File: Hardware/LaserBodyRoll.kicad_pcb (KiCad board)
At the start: 2 copper layers, 85 parts, among them J1 CONN_01X02, J2 FTSH-105-01-L-DV-K, J4 CONN_01X06, J5 CONN_01X02, J6 CONN_01X02, J7 CONN_01X06, J8 Raspberry_Pi_2_3, Q1 Q_NPN_BCE, Q2 Q_NPN_BCE, Q3 Q_NPN_BCE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

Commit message: Updated the board outline and placement of parts.
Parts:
- removed C6: 0.1u, Capacitors_SMD:C_0603
- removed J7: CONN_01X06, Connectors_Phoenix:PhoenixContact_MSTBVA-G_06x5.00mm_Vertical
- added J3: Conn_01x04, Pin_Headers:Pin_Header_Straight_1x04_Pitch2.54mm, F.Cu at (101.4, 78.0)
- added REF**: MountingHole_2.7mm_M2.5, Mounting_Holes:MountingHole_2.7mm_M2.5, F.Cu at (56.0, 67.0)
- added REF**: MountingHole_2.7mm_M2.5, Mounting_Holes:MountingHole_2.7mm_M2.5, F.Cu at (114.0, 44.0)
- added REF**: MountingHole_2.7mm_M2.5, Mounting_Holes:MountingHole_2.7mm_M2.5, F.Cu at (56.0, 44.0)
- added REF**: MountingHole_3.2mm_M3, Mounting_Holes:MountingHole_3.2mm_M3, F.Cu at (140.0, 44.0)
- added REF**: MountingHole_3.2mm_M3, Mounting_Holes:MountingHole_3.2mm_M3, F.Cu at (140.0, 76.0)
- added REF**: MountingHole_3.2mm_M3, Mounting_Holes:MountingHole_3.2mm_M3, F.Cu at (44.0, 76.0)
- added REF**: MountingHole_3.2mm_M3, Mounting_Holes:MountingHole_3.2mm_M3, F.Cu at (44.0, 44.0)
- added TP1: Test_Point, Connectors_TestPoints:Test_Point_Pad_d2.0mm, F.Cu at (53.0, 78.0)
- added TP2: Test_Point, Connectors_TestPoints:Test_Point_Pad_d2.0mm, F.Cu at (49.0, 50.0)
- added TP3: Test_Point, Connectors_TestPoints:Test_Point_Pad_d2.0mm, F.Cu at (61.0, 49.5)
- added TP4: Test_Point, Connectors_TestPoints:Test_Point_Pad_d2.0mm, F.Cu at (98.0, 51.5)
- added TP5: Test_Point, Connectors_TestPoints:Test_Point_Pad_d2.0mm, F.Cu at (102.5, 51.5)
- D7, D8: footprint Diodes_SMD:D_SMC -> Diodes_SMD:D_SMB
- J1: footprint Connectors_Phoenix:PhoenixContact_MSTBVA-G_02x5.00mm_Vertical -> Pin_Headers:Pin_Header_Straight_1x02_Pitch2.54mm
- J4: value CONN_01X06 -> Conn_01x04; footprint Connectors_Phoenix:PhoenixContact_MSTBVA-G_06x5.00mm_Vertical -> Pin_Headers:Pin_Header_Straight_1x04_Pitch2.54mm
- W14: footprint Measurement_Points:Measurement_Point_Round-SMD-Pad_Small -> Connectors_TestPoints:Test_Point_Pad_d2.0mm
- moved R11 189.9 mm to (79.5, 77.8), turned to 270 degrees
- moved C13 187.8 mm to (81.5, 77.8), turned to 270 degrees
- moved R29 185.8 mm to (84.0, 77.5), turned to 90 degrees
- moved R2 183.6 mm to (86.5, 77.5), turned to 90 degrees
- moved C11 180.1 mm to (106.5, 62.0)
- moved U3 175.7 mm to (87.0, 63.5)
- moved R12 173.2 mm to (79.5, 69.2), turned to 90 degrees
- moved C14 171.8 mm to (81.5, 69.2), turned to 90 degrees
- moved D7 171.7 mm to (97.8, 67.0)
- moved R30 169.4 mm to (84.0, 69.0), turned to 270 degrees
- moved C12 168.9 mm to (113.5, 62.0)
- moved R1 167.4 mm to (86.5, 69.0), turned to 270 degrees
- moved D8 165.6 mm to (90.5, 75.7), turned to 270 degrees
- moved R13 163.1 mm to (98.5, 71.8)
- moved R14 163.1 mm to (103.5, 71.8)
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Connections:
- J4 pad 1: /IO/12V -> /IO/DOUT1
- J4 pad 2: GND -> /IO/DOUT2
- J4 pad 3: /IO/ANA_OUT1 -> /IO/DIN1
- J4 pad 4: /IO/ANA_OUT2 -> /IO/DIN2
- U5 pad 14: Net-(C6-Pad1) -> (no net)
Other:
- board outline added: 104 x 40 mm

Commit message: Working on the routing.
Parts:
- added C6: 0.1u, Capacitors_SMD:C_0603, F.Cu at (71.8, 49.5)
- moved TP1 15.0 mm to (68.0, 78.0)
- moved C16 13.7 mm to (74.0, 62.5), turned to 90 degrees
- moved D1 4.61 mm to (44.9, 64.0)
- moved REF** 4.00 mm to (140.0, 72.0)
- moved REF** 4.00 mm to (44.0, 72.0)
- moved C3 2.55 mm to (72.0, 75.5)
- moved J1 2.50 mm to (42.0, 58.0)
- turned C20 to 270 degrees
- turned R6 to 270 degrees
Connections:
- J2 pad 2: GND -> /Processor/SWDIO
- J2 pad 4: GND -> /Processor/SWDCLK
- J2 pad 6: /Processor/SWDIO -> /Processor/SWDV
- J2 pad 7: /Processor/SWDCLK -> GND
- J2 pad 9: Net-(J2-Pad9) -> GND
- J8 pad 5: /Processor/SCLK -> /Processor/SCL
- U5 pad 14: (no net) -> Net-(C6-Pad1)
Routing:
- net VCC: track 0.00 -> 204.4 mm, vias 0 -> 10
- net /IO/12V: track 0.00 -> 172.0 mm, vias 0 -> 4
- net /Processor/ICM_INT: track 0.00 -> 62.8 mm, vias 0 -> 1
- net /Processor/SCL: track 0.00 -> 53.3 mm, vias 0 -> 4
- net +5V: track 0.00 -> 45.1 mm
- net Net-(C13-Pad1): track 0.00 -> 44.6 mm, vias 0 -> 2
- net /Processor/SDA: track 0.00 -> 39.3 mm, vias 0 -> 2
- net /IO/CPU_ANA_OUT2: track 0.00 -> 36.2 mm, vias 0 -> 2
- net Net-(C14-Pad1): track 0.00 -> 35.2 mm
- net Net-(R2-Pad1): track 0.00 -> 28.7 mm, vias 0 -> 2
- net /IO/DIN2: track 0.00 -> 23.6 mm
- net Net-(C11-Pad1): track 0.00 -> 22.6 mm
- net /Processor/VL53L0X_GP: track 0.00 -> 21.3 mm
- net /IO/DIN1: track 0.00 -> 21.0 mm
- net Net-(C12-Pad1): track 0.00 -> 20.1 mm
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- added copper zone on F.Cu, net +5V
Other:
- rule trace_min: 0.2 -> 0.1524

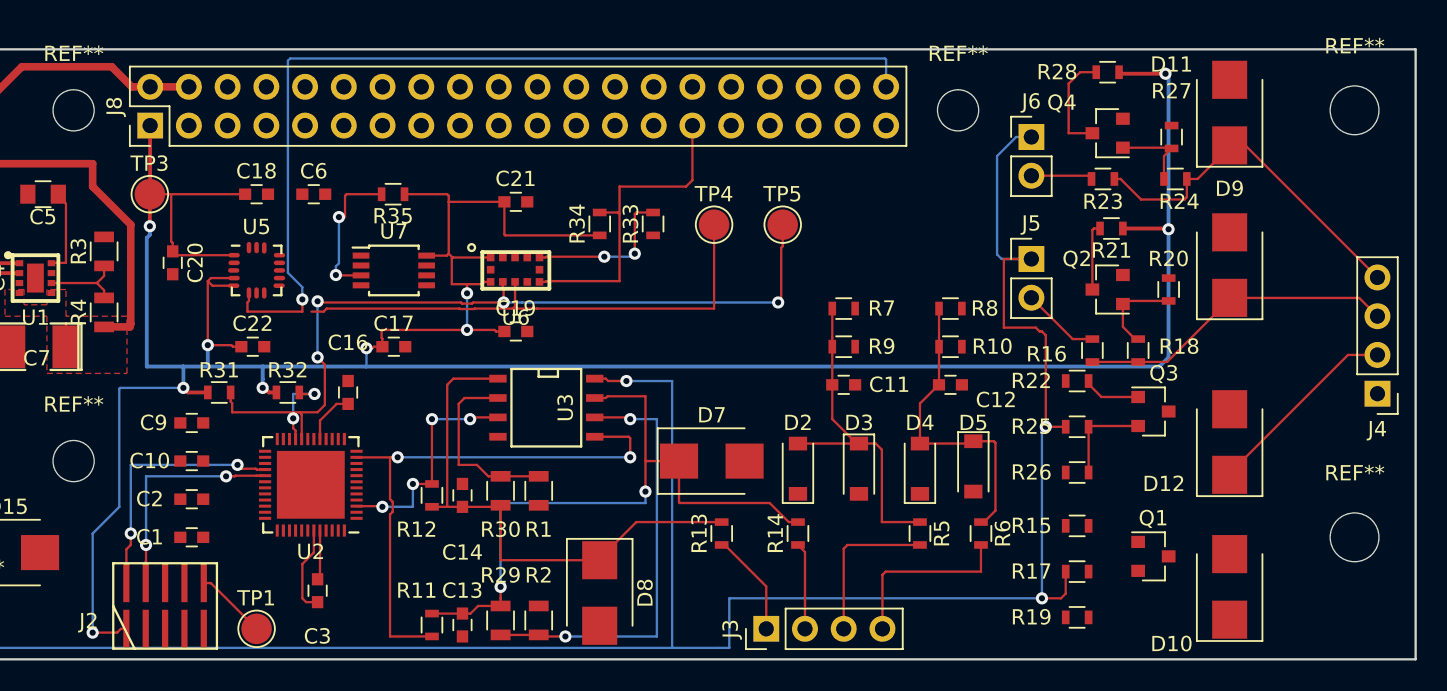
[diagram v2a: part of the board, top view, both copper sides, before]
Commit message: Partial routing, but it is starting to look weird. I'm going to try and change the pinout of the PSoC to make routing easier.
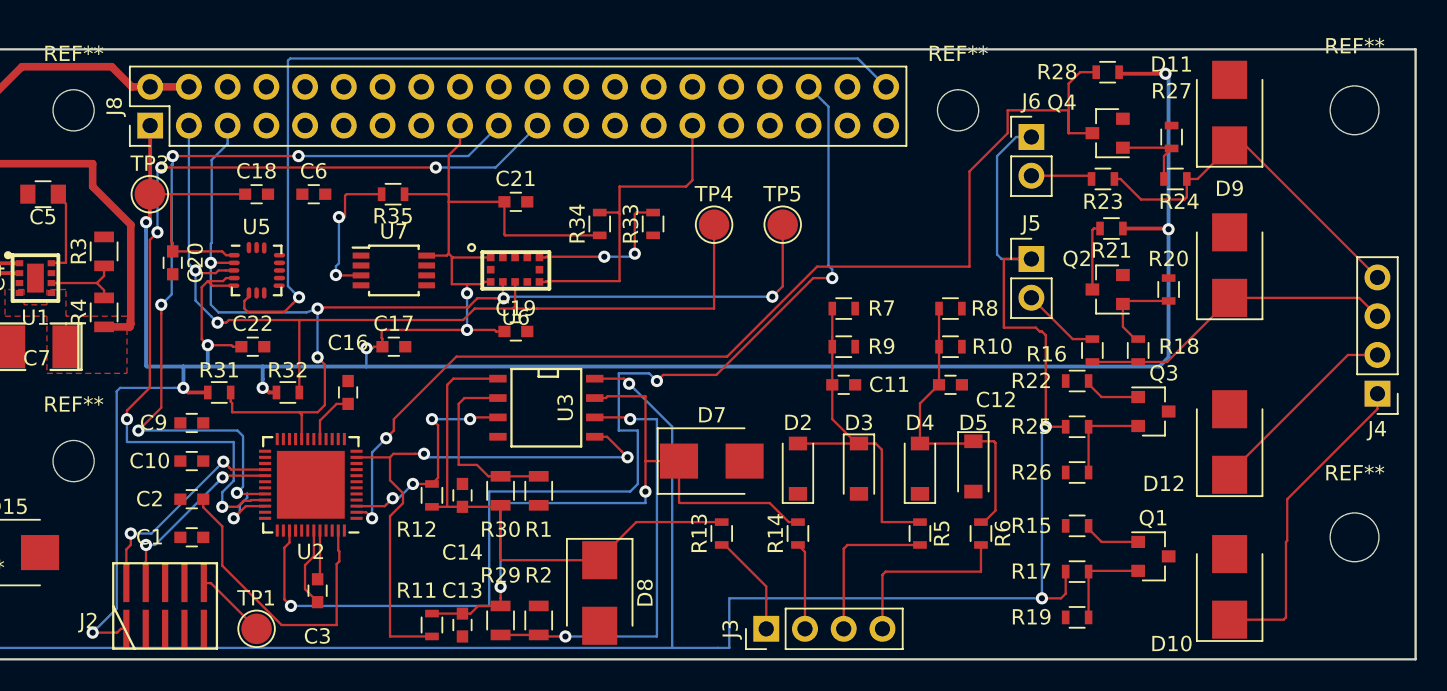
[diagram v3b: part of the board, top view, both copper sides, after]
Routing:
- net /Processor/GP1: track 0.00 -> 74.4 mm, vias 0 -> 3
- net /IO/CPU_DIN2: track 6.92 -> 73.9 mm, vias 0 -> 2
- net /Processor/MISO: track 0.00 -> 59.4 mm, vias 0 -> 5
- net /Processor/MOSI: track 0.00 -> 54.0 mm, vias 0 -> 5
- net /Processor/SDA: track 39.3 -> 61.4 mm
- net /IO/DOUT1: track 0.00 -> 20.9 mm
- net Net-(C2-Pad1): track 0.00 -> 20.3 mm
- net /Processor/SCL: track 53.3 -> 73.2 mm, vias 4 -> 5
- net Net-(Q1-Pad2): track 0.00 -> 6.27 mm
- net VCC: track 204.4 -> 209.7 mm
- net /Processor/SCLK: track 0.00 -> 4.39 mm, vias 0 -> 1
- net Net-(Q1-Pad1): track 0.00 -> 3.80 mm
- net /Processor/SWDCLK: track 14.8 -> 12.2 mm
- net /Processor/SWDIO: track 16.8 -> 14.3 mm
- net /IO/12V: track 172.0 -> 170.2 mm
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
